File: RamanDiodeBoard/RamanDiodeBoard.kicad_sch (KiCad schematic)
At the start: 13 parts, among them Q1 BSS138, Q2 BSS138

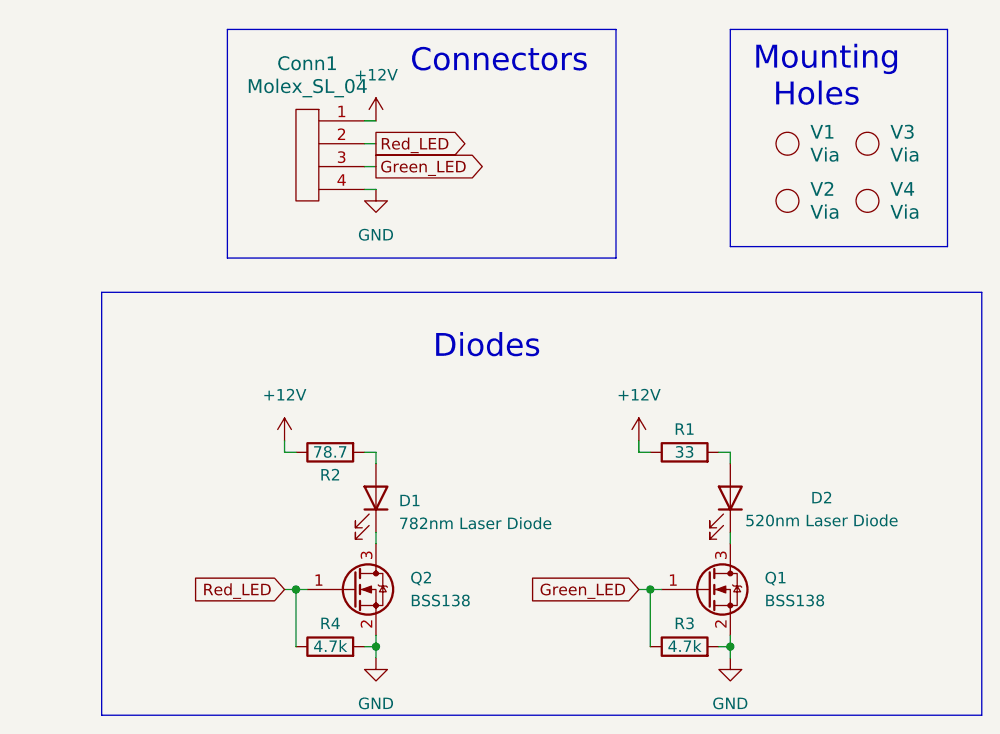
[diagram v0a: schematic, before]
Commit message: laser diode board changes
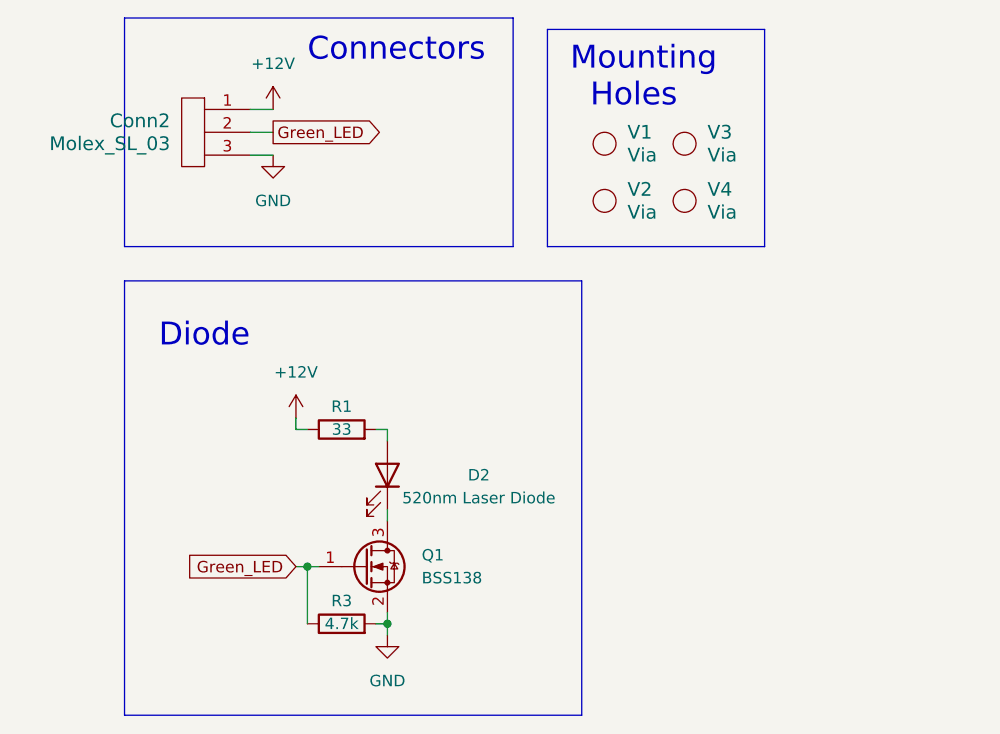
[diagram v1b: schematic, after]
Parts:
- removed Conn1: Molex_SL_04, MRDT_Connectors:MOLEX_SL_04_Vertical, symbol MRDT_Connectors:Molex_SL_04
- removed D1: 782nm Laser Diode, Package_TO_SOT_THT:TO-18-3, symbol Device:LED
- removed Q2: BSS138, Package_TO_SOT_SMD:SOT-23, symbol Transistor_FET:BSS138
- removed R2: 78.7, Resistor_SMD:R_1206_3216Metric_Pad1.30x1.75mm_HandSolder, symbol Device:R
- removed R4: 4.7k, Resistor_SMD:R_0603_1608Metric_Pad0.98x0.95mm_HandSolder, symbol Device:R
- added Conn2: Molex_SL_03, MRDT_Connectors:MOLEX_SL_03_Vertical, symbol MRDT_Connectors:Molex_SL_03
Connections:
- net +12V: now also Conn2.1
- net GND: now also Conn2.3
- net Green_LED: now also Conn2.2
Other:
- note added: "Diode"
- note removed: "Diodes"
- moved on the sheet: D2, Q1, R1, R3, V1, V2, V3, V4
